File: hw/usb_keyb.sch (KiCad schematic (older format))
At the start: 127 parts, among them J1 POWER, J10 SPI, J11 ZX-BUS, J14 RJ45-TRANSFO, J2 Micro_SD_Card, J3 USB_1, J5 MX_ROW, J6 MX_COL, J7 I2C, J8 UART, J9 PROG, SW1 RESET, U1 LM3671MF, U2 STM32F407VETx, U3 STMPS2141STR, U4 STMPS2141STR, U5 DP83848C, Y1 8MHz, Y2 50MHz

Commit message: no message
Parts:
- removed J11: ZX-BUS, Connectors_IEC_DIN:Socket_DIN41612-CaseC1-AC-Female-64Pin-2rows, symbol Conn_02x32_Row_Letter_Last
- added J4: ZX-BUS, Projects:Socket_DIN41612-CaseC1-AB-Female-56Pin-2rows, symbol Conn_02x28_Row_Letter_Last
- J3: footprint w_conn_pc:conn_usb_Ax2 -> Projects:conn_usb_Ax2
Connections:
- net labels added: FSMC_A16, FSMC_D0, FSMC_D1, FSMC_D10, FSMC_D11, FSMC_D12, FSMC_D13, FSMC_D14, FSMC_D15, FSMC_D2, FSMC_D3, FSMC_D4, FSMC_D5, FSMC_D6, FSMC_D7, FSMC_D8, FSMC_D9, FSMC_NE1, FSMC_NOE, FSMC_NWE
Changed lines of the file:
@@
 EESchema Schematic File Version 2
-LIBS:usb_keyb-rescue
+LIBS:mem
 LIBS:power
 LIBS:device
@@
 LIBS:contrib
 LIBS:valves
-LIBS:stm32
-LIBS:stm_var
 LIBS:usb_keyb-cache
 EELAYER 25 0
@@
 	1    0    0    -1
 $EndComp
-$Comp
-L Conn_02x32_Row_Letter_Last J11
-U 1 1 5ABDA855
-P 13500 3850
-F 0 "J11" H 13550 5450 50  0000 C CNN
-F 1 "ZX-BUS" H 13550 2150 50  0000 C CNN
-F 2 "Connectors_IEC_DIN:Socket_DIN41612-CaseC1-AC-Female-64Pin-2rows" H 13500 3850 50  0001 C CNN
-F 3 "" H 13500 3850 50  0001 C CNN
-	1    13500 3850
-	1    0    0    -1
-$EndComp
 Text GLabel 12450 1650 2    60   Input ~ 0
 ZIORQn
@@
 F 0 "J3" H 5075 1600 50  0000 L CNN
 F 1 "USB_1" H 4750 1600 50  0000 L CNN
-F 2 "w_conn_pc:conn_usb_Ax2" H 5100 1200 50  0001 C CNN
+F 2 "Projects:conn_usb_Ax2" H 5100 1200 50  0001 C CNN
 F 3 "" H 5100 1200 50  0001 C CNN
 	1    4950 1250
@@
 Text GLabel 10750 4650 2    60   Input ~ 0
 RX
+$Comp
+L Conn_02x28_Row_Letter_Last J4
+U 1 1 5AB497AB
+P 13500 3650
+F 0 "J4" H 13550 5050 50  0000 C CNN
+F 1 "ZX-BUS" H 13550 2150 50  0000 C CNN
+F 2 "Projects:Socket_DIN41612-CaseC1-AB-Female-56Pin-2rows" H 13500 3650 50  0001 C CNN
+F 3 "" H 13500 3650 50  0001 C CNN
+	1    13500 3650
+	1    0    0    -1
+$EndComp
+Text GLabel 1750 8450 0    60   Input ~ 0
+FSMC_D0
+Text GLabel 1750 8550 0    60   Input ~ 0
+FSMC_D1
+Text GLabel 1750 7050 0    60   Input ~ 0
+FSMC_D2
+Text GLabel 1750 7150 0    60   Input ~ 0
+FSMC_D3
+Text GLabel 1750 6050 0    60   Input ~ 0
+FSMC_D4
+Text GLabel 1750 6150 0    60   Input ~ 0
+FSMC_D5
+Text GLabel 1750 6250 0    60   Input ~ 0
+FSMC_D6
+Text GLabel 1750 6350 0    60   Input ~ 0
+FSMC_D7
+Text GLabel 1750 6450 0    60   Input ~ 0
+FSMC_D8
+Text GLabel 1750 6550 0    60   Input ~ 0
+FSMC_D9
+Text GLabel 1750 6650 0    60   Input ~ 0
+FSMC_D10
+Text GLabel 1750 6750 0    60   Input ~ 0
+FSMC_D11
+Text GLabel 1750 6850 0    60   Input ~ 0
+FSMC_D12
+Text GLabel 1750 7850 0    60   Input ~ 0
+FSMC_D13
+Text GLabel 1750 7950 0    60   Input ~ 0
+FSMC_D14
+Text GLabel 1750 8050 0    60   Input ~ 0
+FSMC_D15
+Text GLabel 1750 7450 0    60   Input ~ 0
+FSMC_NOE
+Text GLabel 1750 7550 0    60   Input ~ 0
+FSMC_NWE
+Text GLabel 1750 7750 0    60   Input ~ 0
+FSMC_NE1
+Text GLabel 1750 8150 0    60   Input ~ 0
+FSMC_A16
 $EndSCHEMATC

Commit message: Схема и плата обновлены до актуальной версии
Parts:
- removed C19, C20, C21, C22, C24, C25, C26, C27, C29, C30, C31: 100n, Capacitors_SMD:C_0805, symbol C
- removed C23, C28: 10u, Capacitors_Tantalum_SMD:CP_Tantalum_Case-A_EIA-3216-18_Reflow, symbol CP
- removed J14: RJ45-TRANSFO, Projects:rj45_wurth-7499211122a, symbol RJ45-TRANSFO-RESCUE-usb_keyb
- removed L2: 2.2µH, Inductors_SMD:L_0805, symbol L
- removed R59, R60, R62, R63: 2k, Resistors_SMD:R_0805, symbol R
- removed R61: 10k, Resistors_SMD:R_0805, symbol R
- removed R64: 4k7, Resistors_SMD:R_0805, symbol R
- removed R65: 150, Resistors_SMD:R_0805, symbol R
- removed R66: 18, Resistors_SMD:R_0805, symbol R
- removed R67, R68, R69, R70: 51, Resistors_SMD:R_0805, symbol R
- removed R71, R72: 330, Resistors_SMD:R_0805, symbol R
- removed U5: DP83848C, Housings_QFP:LQFP-48_7x7mm_Pitch0.5mm, symbol DP83848C
- removed Y2: 50MHz, Crystals:Crystal_SMD_7050-4pin_7.0x5.0mm, symbol Crystal_GND24
- added J11: RMII, symbol Conn_02x10_Odd_Even
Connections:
- net labels removed: LA, LL, PFB, RD+, RD-, RX, TD+, TD-, TX, UART_CTS, UART_RTS
- wire segments 247 -> 160

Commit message: Схема обновлена до актуальной версии.
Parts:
- added J12: PS2, symbol Conn_01x04
- added R59, R60, R61, R62, R63, R64, R65, R66, R67, R68, R69, R70, R71, R72: 10k, Resistors_SMD:R_0805, symbol R
- added SW2: OUTPUT, symbol SW_DIP_x06
- added SW3: MATRIX, symbol SW_DIP_x08
- added U5: 74LS245, symbol 74LS245
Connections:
- net labels added: D4, D5, D6, D7, MTX0, MTX1, MTX2, MTX3, MTX4, MTX5, MTX6, MTX7, OUT0, OUT1, OUT2, OUT3, OUT4, OUT5, PS2_CLK, PS2_DAT, ZB_DIR
- net labels removed: +5, PA4, PA8
- wire segments 160 -> 220

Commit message: Обновлены плата и схема устройства
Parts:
- removed J8: UART, Socket_Strips:Socket_Strip_Straight_1x06_Pitch2.54mm, symbol Conn_01x06
- removed J9: PROG, Socket_Strips:Socket_Strip_Straight_1x05_Pitch2.00mm, symbol Conn_01x05
- removed R32, R33, R34, R35, R44, R45, R46, R47, R62, R63, R64, R65, R66, R67, R68, R69, R70, R71, R72: 10k, Resistors_SMD:R_0805, symbol R
- removed SW2: OUTPUT, symbol SW_DIP_x06
- added J8: UART, Socket_Strips:Socket_Strip_Straight_1x04_Pitch2.54mm, symbol Conn_01x04
- added J9: PROG, Socket_Strips:Socket_Strip_Straight_2x02_Pitch2.00mm, symbol Conn_02x02_Odd_Even
- added R54, R55, R56, R57, R58, R59, R60, R61: 10k, Resistors_SMD:R_0805, symbol R
- added SW2: OUTPUT, Buttons_Switches_THT:SW_DIP_x3_W7.62mm_Slide, symbol SW_DIP_x03
- J11: footprint (none) -> Socket_Strips:Socket_Strip_Straight_2x10_Pitch2.54mm
- J12: footprint (none) -> Socket_Strips:Socket_Strip_Straight_1x04_Pitch2.54mm
- SW3: footprint (none) -> Buttons_Switches_THT:SW_DIP_x8_W7.62mm_Slide
- U5: footprint (none) -> Housings_SOIC:SOIC-20W_7.5x12.8mm_Pitch1.27mm
- renumbered R48 to R24, R49 to R25, R50 to R26, R51 to R27, R52 to R28, R53 to R29, R54 to R30, R55 to R31, R56 to R32, R57 to R33, R58 to R34, R24 to R35, R25 to R36, R26 to R37, R27 to R38, R28 to R39, R29 to R40, R30 to R41, R31 to R42, R36 to R43, R37 to R44, R38 to R45, R39 to R46, R40 to R47, R41 to R48, R42 to R49, R43 to R50, R59 to R51, R60 to R52, R61 to R53
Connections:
- net labels added: LED_1, LED_2, LED_3
- net labels removed: FSMC_A16, FSMC_D0, FSMC_D1, FSMC_D10, FSMC_D11, FSMC_D12, FSMC_D13, FSMC_D14, FSMC_D15, FSMC_D2, FSMC_D3, FSMC_D4, FSMC_D5, FSMC_D6, FSMC_D7, FSMC_D8, FSMC_D9, FSMC_NE1, FSMC_NOE, FSMC_NWE, MC10, MC11, MC8, MC9, MR10, MR11, MR8, MR9, OUT3, OUT4, OUT5, ZB_DIR
- wire segments 220 -> 200
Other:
- moved on the sheet: J10, J12

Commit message: Обновлена плата
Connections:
- net labels added: FS_N, FS_P, F_N, F_P, HS_N, HS_P, H_N, H_P, SD0, SD1, SD2, SD3
- net labels removed: FS_D+, FS_D-, HS_D+, HS_D-
- wire segments 200 -> 201
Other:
- moved on the sheet: R14
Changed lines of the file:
@@
 L R R14
 U 1 1 5AAFEBEA
-P 4500 1150
-F 0 "R14" V 4550 1350 50  0000 C CNN
-F 1 "22" V 4500 1150 50  0000 C CNN
-F 2 "Resistors_SMD:R_0805" V 4430 1150 50  0001 C CNN
-F 3 "" H 4500 1150 50  0001 C CNN
-	1    4500 1150
+P 4225 1150
+F 0 "R14" V 4275 1350 50  0000 C CNN
+F 1 "22" V 4225 1150 50  0000 C CNN
+F 2 "Resistors_SMD:R_0805" V 4155 1150 50  0001 C CNN
+F 3 "" H 4225 1150 50  0001 C CNN
+	1    4225 1150
 	0    -1   -1   0
 $EndComp
@@
 $EndComp
 Text GLabel 3925 1250 0    60   Input ~ 0
-FS_D-
+FS_N
 Text GLabel 3925 1150 0    60   Input ~ 0
-FS_D+
+FS_P
 $Comp
 L GND #PWR04
@@
 FS_PWR
 Text GLabel 10750 4750 2    60   Input ~ 0
-FS_D-
+FS_N
 Text GLabel 10750 4850 2    60   Input ~ 0
-FS_D+
+FS_P
 $Comp
 L +3.3V #PWR06
@@
 HS_PWR
 Text GLabel 10750 7950 2    60   Input ~ 0
-D1
+SD1
 Text GLabel 10750 8050 2    60   Input ~ 0
-D2
+SD2
 Text GLabel 10750 7850 2    60   Input ~ 0
-D0
+SD0
 Text GLabel 10750 8150 2    60   Input ~ 0
-D3
+SD3
 Text GLabel 10750 8250 2    60   Input ~ 0
 CK
@@
 $EndComp
 Text GLabel 8400 1600 0    60   Input ~ 0
-D2
+SD2
 Text GLabel 8400 1700 0    60   Input ~ 0
-D3
+SD3
 Text GLabel 8400 1800 0    60   Input ~ 0
 CMD
 Text GLabel 8400 2200 0    60   Input ~ 0
-D0
+SD0
 Text GLabel 8400 2300 0    60   Input ~ 0
-D1
+SD1
 Text GLabel 8400 2000 0    60   Input ~ 0
 CK
@@
 U 1 1 5AB23AFB
 P 4225 1600
-F 0 "R16" V 4275 1425 50  0000 C CNN
+F 0 "R16" V 4275 1800 50  0000 C CNN
 F 1 "22" V 4225 1600 50  0000 C CNN
 F 2 "Resistors_SMD:R_0805" V 4155 1600 50  0001 C CNN
@@
 $EndComp
 Text GLabel 3925 1700 0    60   Input ~ 0
-HS_D-
+HS_N
 Text GLabel 3925 1600 0    60   Input ~ 0
-HS_D+
+HS_P
 $Comp
 L +3.3V #PWR024
@@
 $EndComp
 Text GLabel 10750 6750 2    60   Input ~ 0
-HS_D-
+HS_N
 Text GLabel 10750 6850 2    60   Input ~ 0
-HS_D+
+HS_P
 Text GLabel 10750 5150 2    60   Input ~ 0
 SPI_CS
@@
 Wire Wire Line
 	4075 1250 3925 1250
-Wire Wire Line
-	3925 1150 4350 1150
 Connection ~ 1700 9850
 Wire Wire Line
@@
 	1    0    0    -1
 $EndComp
+Wire Wire Line
+	4375 1150 4650 1150
+Wire Wire Line
+	3925 1150 4075 1150
+Text Label 4400 1150 0    60   ~ 0
+F_P
+Text Label 4400 1250 0    60   ~ 0
+F_N
+Text Label 4400 1600 0    60   ~ 0
+H_P
+Text Label 4400 1700 0    60   ~ 0
+H_N
 $EndSCHEMATC

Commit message: Обновлены назначение выводов и плата
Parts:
- removed C18: 4,7uF, Capacitors_Tantalum_SMD:CP_Tantalum_Case-A_EIA-3216-18_Reflow, symbol CP
- removed J1: POWER, Connectors_Phoenix:PhoenixContact_GMSTBA-G_04x7.50mm_Angled, symbol Conn_01x04
- removed JP1, JP2: 5Vin, Pin_Headers:Pin_Header_Straight_1x02_Pitch2.54mm, symbol Jumper_NC_Small
- removed JP3: 3Vin, Pin_Headers:Pin_Header_Straight_1x02_Pitch2.54mm, symbol Jumper_NC_Small
- removed R11: 0, Resistors_SMD:R_0805, symbol R
- removed R13: 10k, Resistors_SMD:R_0805, symbol R
- removed U4: STMPS2141STR, TO_SOT_Packages_SMD:SOT-23-5, symbol STMPS2141STR
- added C18, C19: 2,2u, Capacitors_SMD:C_0402, symbol C
- added C20, C21, C22, C23, C24, C25: NFM21PC104R1E3D, Projects:NFM21P, symbol EMI_Filter_C
- added FL1, FL2: DLW21SN371SQ2, Projects:DLW21S, symbol EMI_Filter_CommonMode
- C13: value 100uF -> 10uF; footprint Capacitors_SMD:CP_Elec_5x5.7 -> Capacitors_Tantalum_SMD:CP_Tantalum_Case-A_EIA-3216-18_Reflow
- R14, R15, R16, R17: footprint Resistors_SMD:R_0805 -> Resistors_SMD:R_0402
- U3: value STMPS2141STR -> STMPS2161STR
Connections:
- net labels added: F1_N, F1_P, F2_N, F2_P, H1_N, H1_P, H2_N, H2_P, USB_PWR, VCC
- net labels removed: FS_PWR, F_N, F_P, HS_PWR, H_N, H_P, VR+
- wire segments 201 -> 203
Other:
- moved on the sheet: C12, C17, J3, R10, R12, R14, R15, R16, R17, U3

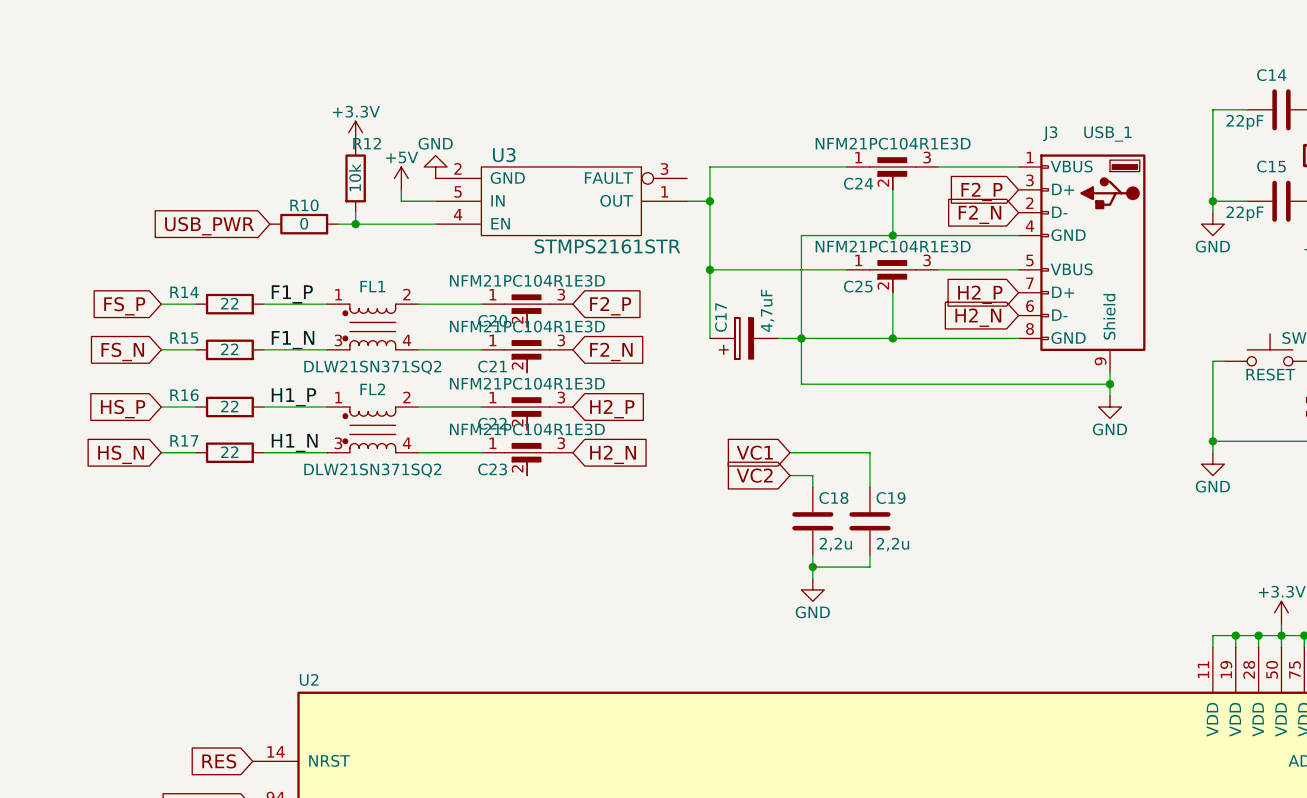
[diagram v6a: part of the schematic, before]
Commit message: Обновлена схема защиты USB
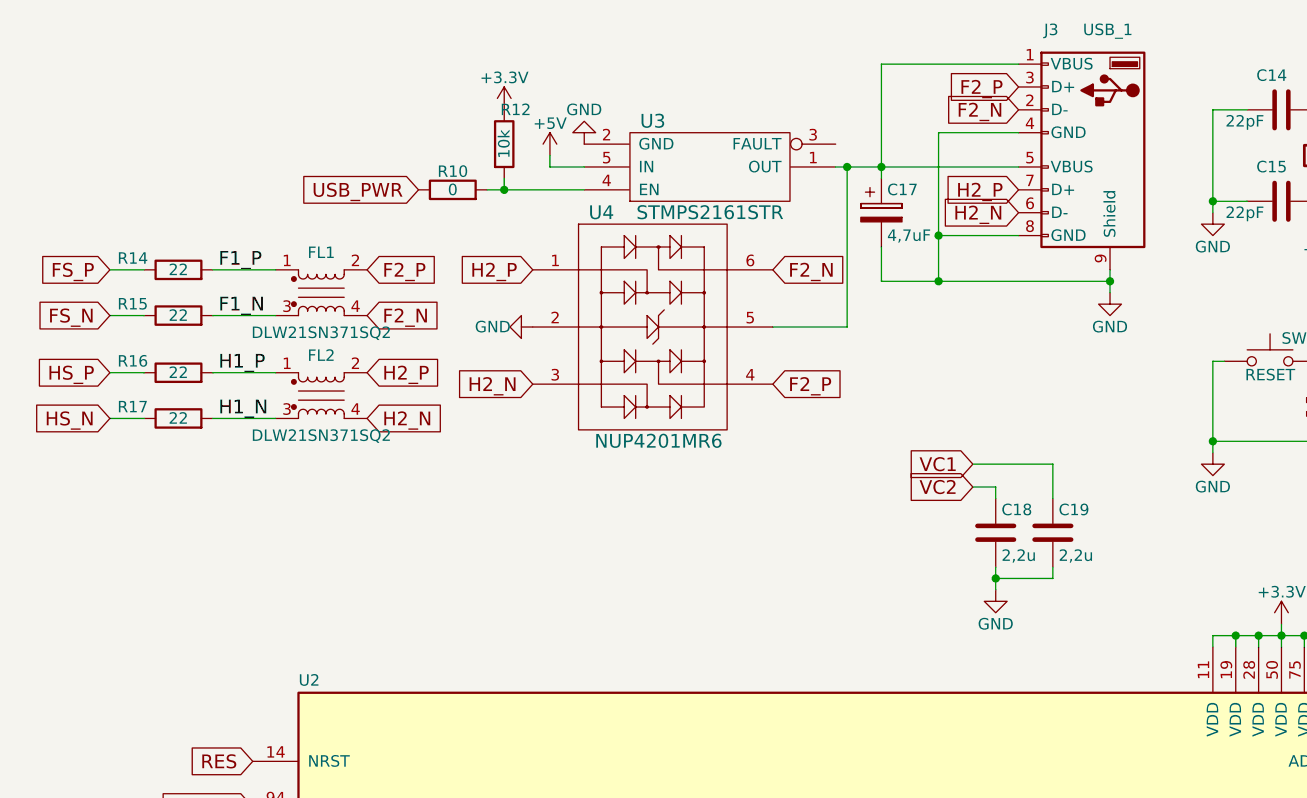
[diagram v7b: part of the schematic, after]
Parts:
- removed C20, C21, C22, C23, C24, C25: NFM21PC104R1E3D, Projects:NFM21P, symbol EMI_Filter_C
- added U4: NUP4201MR6, TO_SOT_Packages_SMD:TSOT-23-6, symbol NUP4201MR6
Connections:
- net F2_N: now also FL1.4, U4.6
- net F2_P: now also FL1.2, U4.4
- net GND: now also U4.2
- net H2_N: now also FL2.4, U4.3
- net H2_P: now also FL2.2, U4.1
- net at J3.1 (VBUS): now also C17.1, J3.5 (VBUS), U3.1 (OUT), U4.5
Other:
- moved on the sheet: C17, C18, C19, FL1, FL2, J3, R10, R12, R14, R15, R16, R17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

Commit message: Обновлена плата
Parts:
- added D1: L1, LEDs:LED_0805, symbol LED
- added D2: L2, LEDs:LED_0805, symbol LED
- added D3: ERR, LEDs:LED_0805, symbol LED
- added J13: OUT_JMP, Pin_Headers:Pin_Header_Straight_1x03_Pitch2.54mm, symbol Conn_01x03
- added J14: MTX_JMP, Pin_Headers:Pin_Header_Straight_1x08_Pitch2.54mm, symbol Conn_01x08
- added R12, R13, R62: 10k, Resistors_SMD:R_0805, symbol R
- renumbered R12 to R11
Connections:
- net GND: now also D1.1 (K), D2.1 (K), D3.1 (K), J13.1 (Pin_1), J13.2 (Pin_2), J13.3 (Pin_3), J14.1 (Pin_1), J14.2 (Pin_2), J14.3 (Pin_3), J14.4 (Pin_4), J14.5 (Pin_5), J14.6 (Pin_6), J14.7 (Pin_7), J14.8 (Pin_8)
- net LED_1: now also U2.67 (I2C3_SCL/RCC_MCO_1/TIM1_CH1/USART1_CK/USB_OTG_FS_SOF/PA8), R12.1; no longer U2.35 (ADC1_IN8/ADC2_IN8/ETH_RXD2/TIM1_CH2N/TIM3_CH3/TIM8_CH2N/USB_OTG_HS_ULPI_D1/PB0)
- net LED_2: now also U2.68 (DAC_EXTI9/DCMI_D0/I2C3_SMBA/TIM1_CH2/USART1_TX/USB_OTG_FS_VBUS/PA9), R13.1; no longer U2.36 (ADC1_IN9/ADC2_IN9/ETH_RXD3/TIM1_CH3N/TIM3_CH4/TIM8_CH3N/USB_OTG_HS_ULPI_D2/PB1)
- net LED_3: now also U2.69 (DCMI_D1/TIM1_CH3/USART1_RX/USB_OTG_FS_ID/PA10), R62.1; no longer U2.37 (BOOT1/PB2)
- net OUT0: now also U2.35 (ADC1_IN8/ADC2_IN8/ETH_RXD2/TIM1_CH2N/TIM3_CH3/TIM8_CH2N/USB_OTG_HS_ULPI_D1/PB0); no longer U2.67 (I2C3_SCL/RCC_MCO_1/TIM1_CH1/USART1_CK/USB_OTG_FS_SOF/PA8)
- net OUT1: now also U2.36 (ADC1_IN9/ADC2_IN9/ETH_RXD3/TIM1_CH3N/TIM3_CH4/TIM8_CH3N/USB_OTG_HS_ULPI_D2/PB1); no longer U2.68 (DAC_EXTI9/DCMI_D0/I2C3_SMBA/TIM1_CH2/USART1_TX/USB_OTG_FS_VBUS/PA9)
- net OUT2: now also U2.37 (BOOT1/PB2); no longer U2.69 (DCMI_D1/TIM1_CH3/USART1_RX/USB_OTG_FS_ID/PA10)
- new net: D1.2 (A), R12.2
- new net: D2.2 (A), R13.2
- new net: D3.2 (A), R62.2
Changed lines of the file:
@@
 $EndComp
 $Comp
-L R R12
+L R R11
 U 1 1 5AAFE852
 P 2850 950
-F 0 "R12" H 2900 1100 50  0000 C CNN
+F 0 "R11" H 2900 1100 50  0000 C CNN
 F 1 "10k" V 2850 950 50  0000 C CNN
 F 2 "Resistors_SMD:R_0805" V 2780 950 50  0001 C CNN
@@
 Text GLabel 9550 10500 2    60   Input ~ 0
 MTX7
-Text GLabel 10750 4450 2    60   Input ~ 0
+Text GLabel 10750 5350 2    60   Input ~ 0
 OUT0
-Text GLabel 10750 4550 2    60   Input ~ 0
+Text GLabel 10750 5450 2    60   Input ~ 0
 OUT1
-Text GLabel 10750 4650 2    60   Input ~ 0
+Text GLabel 10750 5550 2    60   Input ~ 0
 OUT2
 Text GLabel 10750 3950 2    60   Input ~ 0
@@
 	-1   0    0    -1
 $EndComp
-Text GLabel 10750 5550 2    60   Input ~ 0
+Text GLabel 10750 4650 2    60   Input ~ 0
 LED_3
-Text GLabel 10750 5450 2    60   Input ~ 0
+Text GLabel 10750 4550 2    60   Input ~ 0
 LED_2
-Text GLabel 10750 5350 2    60   Input ~ 0
+Text GLabel 10750 4450 2    60   Input ~ 0
 LED_1
 Text GLabel 13250 7900 0    60   Input ~ 0
@@
 Connection ~ 5500 1550
 Wire Wire Line
-	6250 9800 6200 9800
+	6100 9800 6250 9800
 Wire Wire Line
 	6200 9800 6200 10100
 Wire Wire Line
-	6200 10000 6250 10000
+	6100 10000 6250 10000
 Connection ~ 6200 10000
 Wire Wire Line
-	6200 9900 6250 9900
+	6100 9900 6250 9900
 Connection ~ 6200 9900
 Connection ~ 7100 9350
@@
 Connection ~ 7100 10000
 Wire Wire Line
-	8100 9800 8050 9800
+	7950 9800 8100 9800
 Wire Wire Line
 	8050 9800 8050 10550
 Wire Wire Line
-	8050 10300 8100 10300
+	7950 10300 8100 10300
 Connection ~ 8050 10300
 Wire Wire Line
-	8100 10200 8050 10200
+	7950 10200 8100 10200
 Connection ~ 8050 10200
 Wire Wire Line
-	8050 10100 8100 10100
+	7950 10100 8100 10100
 Connection ~ 8050 10100
 Wire Wire Line
-	8100 10000 8050 10000
+	7950 10000 8100 10000
 Connection ~ 8050 10000
 Wire Wire Line
-	8050 9900 8100 9900
+	7950 9900 8100 9900
 Connection ~ 8050 9900
 Connection ~ 9250 9350
@@
 Connection ~ 9150 10200
 Wire Wire Line
-	8100 10400 8050 10400
+	7950 10400 8100 10400
 Connection ~ 8050 10400
 Wire Wire Line
-	8050 10500 8100 10500
+	7950 10500 8100 10500
 Connection ~ 8050 10500
 Wire Wire Line
@@
 	0    1    1    0
 $EndComp
+$Comp
+L Conn_01x03 J13
+U 1 1 5AC2A39A
+P 5900 9900
+F 0 "J13" H 5900 10100 50  0000 C CNN
+F 1 "OUT_JMP" H 5900 9700 50  0000 C CNN
+F 2 "Pin_Headers:Pin_Header_Straight_1x03_Pitch2.54mm" H 5900 9900 50  0001 C CNN
+F 3 "" H 5900 9900 50  0001 C CNN
+	1    5900 9900
+	-1   0    0    -1
+$EndComp
+Connection ~ 6200 9800
+$Comp
+L Conn_01x08 J14
+U 1 1 5AC2AD3A
+P 7750 10100
+F 0 "J14" H 7750 10500 50  0000 C CNN
+F 1 "MTX_JMP" H 7750 9600 50  0000 C CNN
+F 2 "Pin_Headers:Pin_Header_Straight_1x08_Pitch2.54mm" H 7750 10100 50  0001 C CNN
+F 3 "" H 7750 10100 50  0001 C CNN
+	1    7750 10100
+	-1   0    0    -1
+$EndComp
+Connection ~ 8050 9800
+$Comp
+L LED D1
+U 1 1 5AC306B0
+P 13250 8550
+F 0 "D1" H 13250 8650 50  0000 C CNN
+F 1 "L1" H 13050 8600 50  0000 C CNN
+F 2 "LEDs:LED_0805" H 13250 8550 50  0001 C CNN
+F 3 "" H 13250 8550 50  0001 C CNN
+	1    13250 8550
+	-1   0    0    -1
+$EndComp
+$Comp
+L LED D2
+U 1 1 5AC31005
+P 13250 8750
+F 0 "D2" H 13250 8850 50  0000 C CNN
+F 1 "L2" H 13050 8800 50  0000 C CNN
+F 2 "LEDs:LED_0805" H 13250 8750 50  0001 C CNN
+F 3 "" H 13250 8750 50  0001 C CNN
+	1    13250 8750
+	-1   0    0    -1
+$EndComp
+$Comp
+L LED D3
+U 1 1 5AC31160
+P 13250 8950
+F 0 "D3" H 13250 9050 50  0000 C CNN
+F 1 "ERR" H 13050 9000 50  0000 C CNN
+F 2 "LEDs:LED_0805" H 13250 8950 50  0001 C CNN
+F 3 "" H 13250 8950 50  0001 C CNN
+	1    13250 8950
+	-1   0    0    -1
+$EndComp
+$Comp
+L R R12
+U 1 1 5AC3195A
+P 12950 8550
+F 0 "R12" V 13025 8550 50  0000 C CNN
+F 1 "10k" V 12950 8550 50  0000 C CNN
+F 2 "Resistors_SMD:R_0805" V 12880 8550 50  0001 C CNN
+F 3 "" H 12950 8550 50  0001 C CNN
+	1    12950 8550
+	0    -1   -1   0
+$EndComp
+$Comp
+L R R13
+U 1 1 5AC31EB0
+P 12950 8750
+F 0 "R13" V 13025 8750 50  0000 C CNN
+F 1 "10k" V 12950 8750 50  0000 C CNN
+F 2 "Resistors_SMD:R_0805" V 12880 8750 50  0001 C CNN
+F 3 "" H 12950 8750 50  0001 C CNN
+	1    12950 8750
+	0    -1   -1   0
+$EndComp
+$Comp
+L R R62
+U 1 1 5AC32014
+P 12950 8950
+F 0 "R62" V 13025 8950 50  0000 C CNN
+F 1 "10k" V 12950 8950 50  0000 C CNN
+F 2 "Resistors_SMD:R_0805" V 12880 8950 50  0001 C CNN
+F 3 "" H 12950 8950 50  0001 C CNN
+	1    12950 8950
+	0    -1   -1   0
+$EndComp
+$Comp
+L GND #PWR046
+U 1 1 5AC325BD
+P 13550 9000
+F 0 "#PWR046" H 13550 8750 50  0001 C CNN
+F 1 "GND" H 13550 8850 50  0000 C CNN
+F 2 "" H 13550 9000 50  0001 C CNN
+F 3 "" H 13550 9000 50  0001 C CNN
+	1    13550 9000
+	1    0    0    -1
+$EndComp
+Text GLabel 12800 8950 0    60   Input ~ 0
+LED_3
+Text GLabel 12800 8750 0    60   Input ~ 0
+LED_2
+Text GLabel 12800 8550 0    60   Input ~ 0
+LED_1
+Wire Wire Line
+	13400 8950 13550 8950
+Wire Wire Line
+	13550 8550 13550 9000
+Wire Wire Line
+	13400 8750 13550 8750
+Connection ~ 13550 8950
+Wire Wire Line
+	13400 8550 13550 8550
+Connection ~ 13550 8750
 $EndSCHEMATC
